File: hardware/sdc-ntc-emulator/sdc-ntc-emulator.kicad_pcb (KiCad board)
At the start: 2 copper layers, 104 x 76 mm, 33 parts, among them J1 DevKit J1, J2 DevKit J3, J3 5V IN (RAC03), J4 SDC VE1 / GND, K1 G5V-2-H1 5VDC, Q1 AO3400A, U1 ISO1540, U2 AD5272BRMZ-50

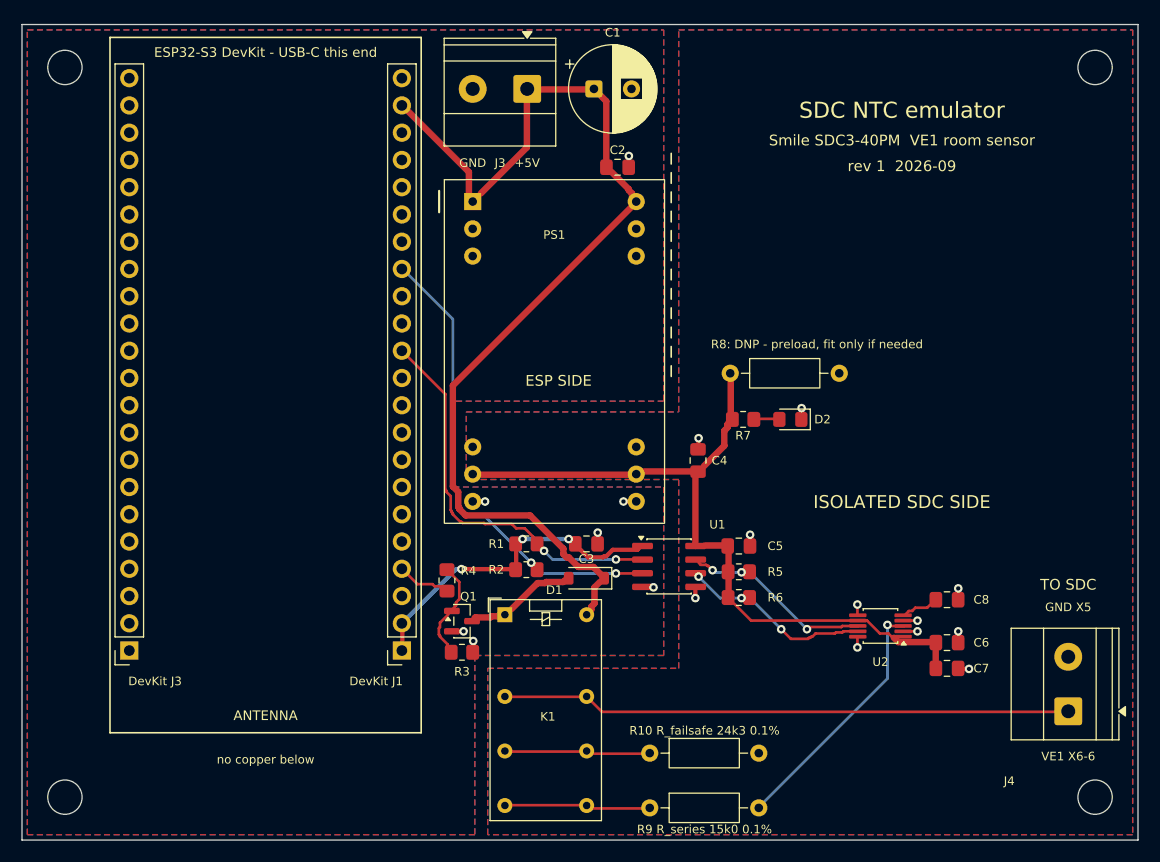
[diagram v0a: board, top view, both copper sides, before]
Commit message: PCB: fit the actual DevKit clone, fix antenna keep-out and GND split
The clone is shorter than the official DevKitC-1 and its module antenna
overhangs the DevKit edge right after pin 1, so the no-copper area now
starts there. That cut the ESP ground pour in two; an explicit GND track
from DevKit J1.22 to the TEM input ground reconnects it. Header row
spacing is now one constant (DEVKIT_ROWS, still 25.4 mm pending a
re-measurement).

Co-Authored-By: Claude Opus 5.5 <noreply@anthropic.com>
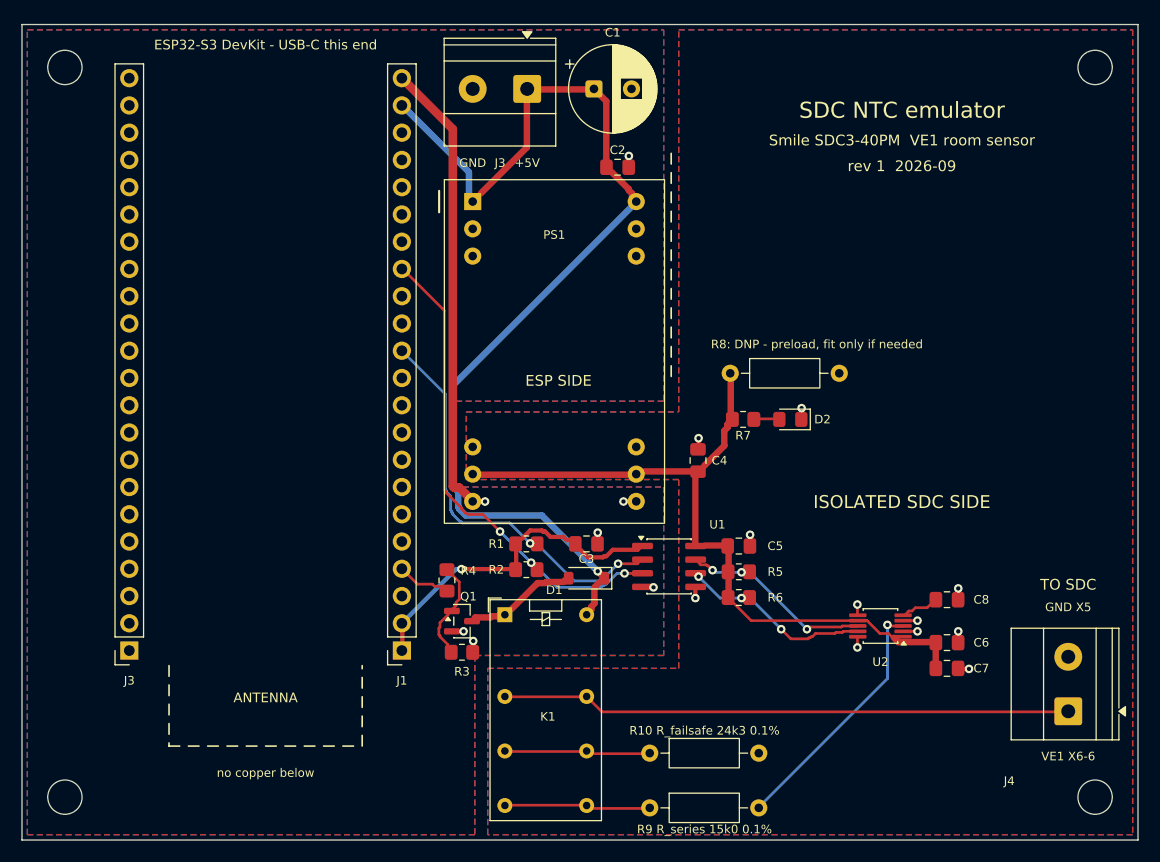
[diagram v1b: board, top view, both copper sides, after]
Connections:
- J2 pad 1: /GND -> unconnected-(J2-Pin_1-Pad1)
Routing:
- net /GND: track 7.90 -> 49.7 mm
- net /SDA_ESP: track 35.4 -> 38.0 mm
- net /SCL_ESP: track 43.9 -> 45.0 mm, vias 2 -> 3
- net /+3V3: track 27.5 -> 28.2 mm, vias 3 -> 1
- net /+5V: track 93.7 -> 93.5 mm, vias 0 -> 1
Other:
- board text added: "J1"
- board text added: "J3"
- board text removed: "DevKit J1"
- board text removed: "DevKit J3"

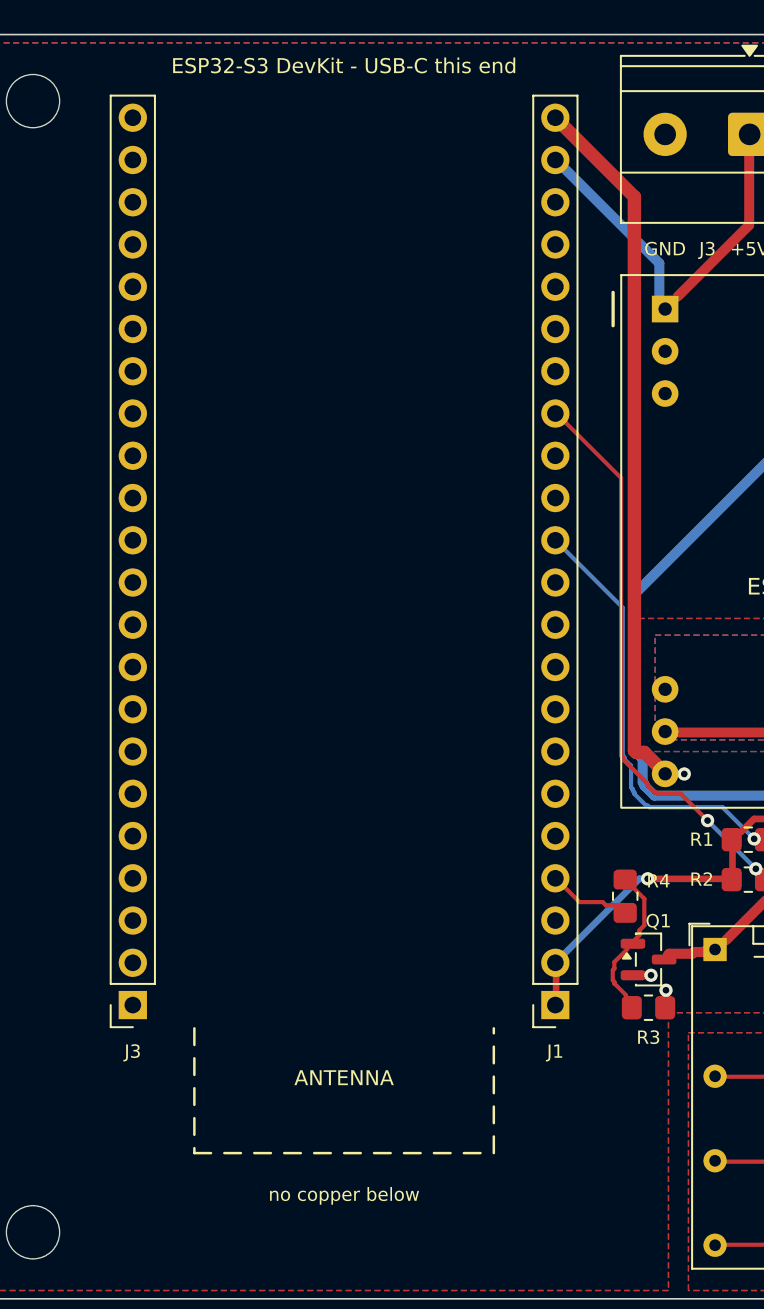
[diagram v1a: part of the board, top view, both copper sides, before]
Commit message: PCB: DevKit header rows 25.1 mm apart (measured)
Co-Authored-By: Claude Opus 5.5 <noreply@anthropic.com>
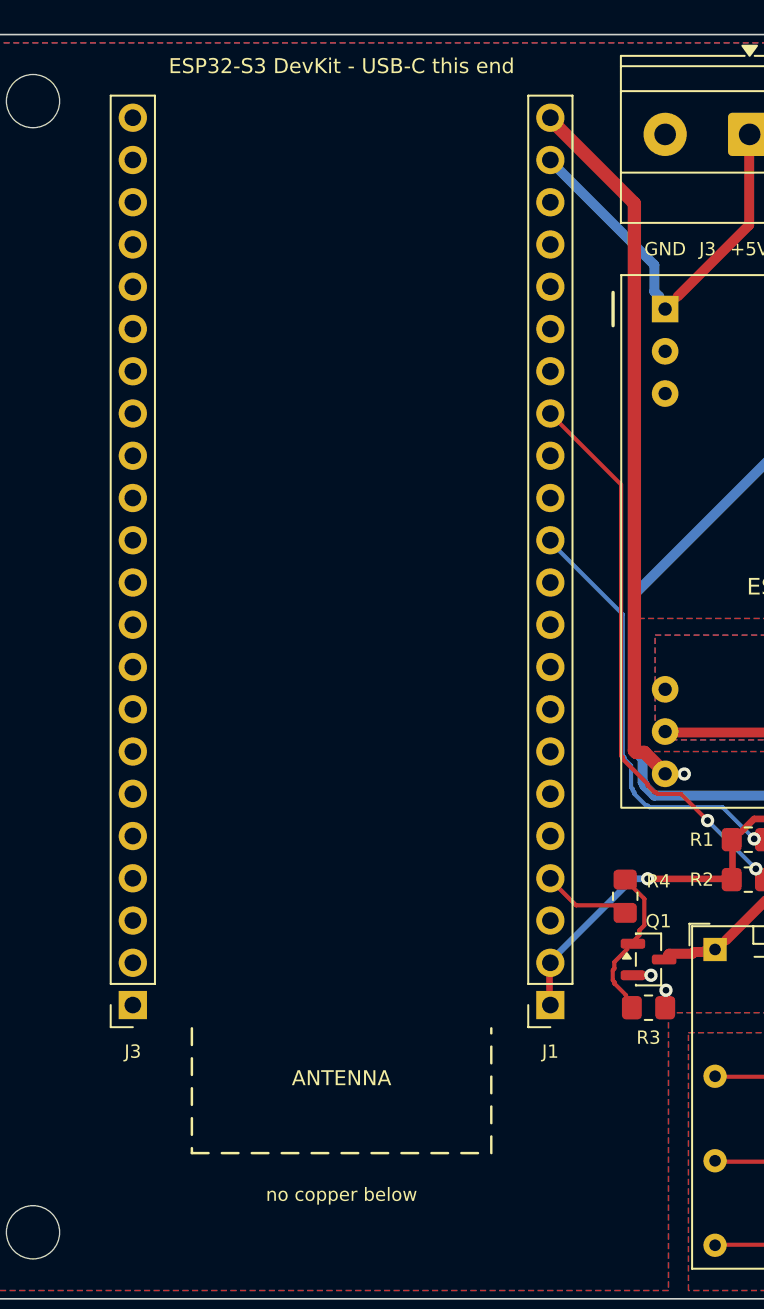
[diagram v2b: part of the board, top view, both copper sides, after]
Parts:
- moved J1 0.30 mm to (135.1, 108.3)

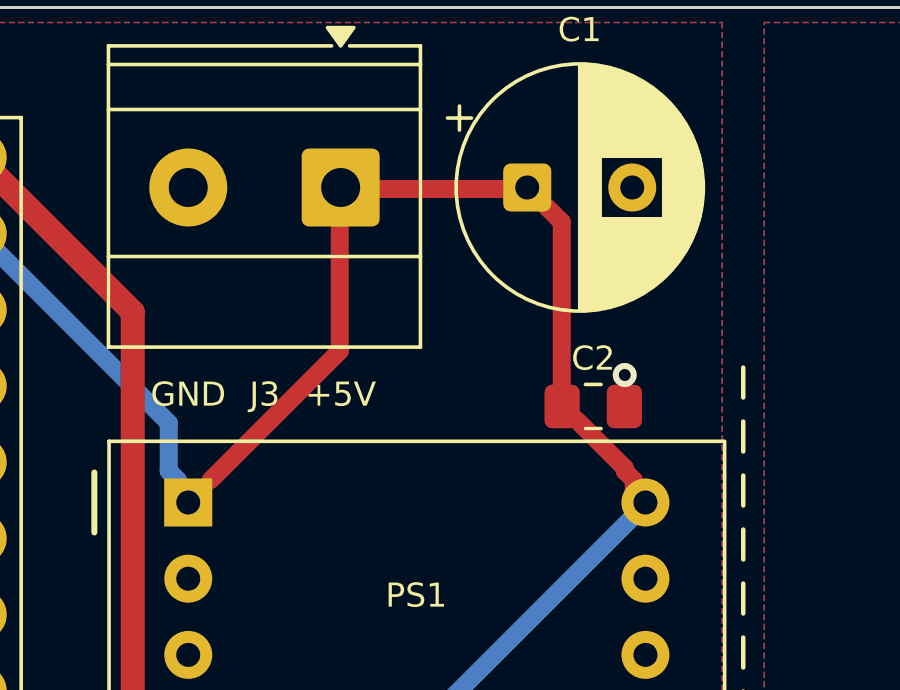
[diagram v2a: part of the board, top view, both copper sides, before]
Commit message: PCB: add 10 uF ceramic (C9) parallel to the 5 V input elco
Co-Authored-By: Claude Opus 5.5 <noreply@anthropic.com>
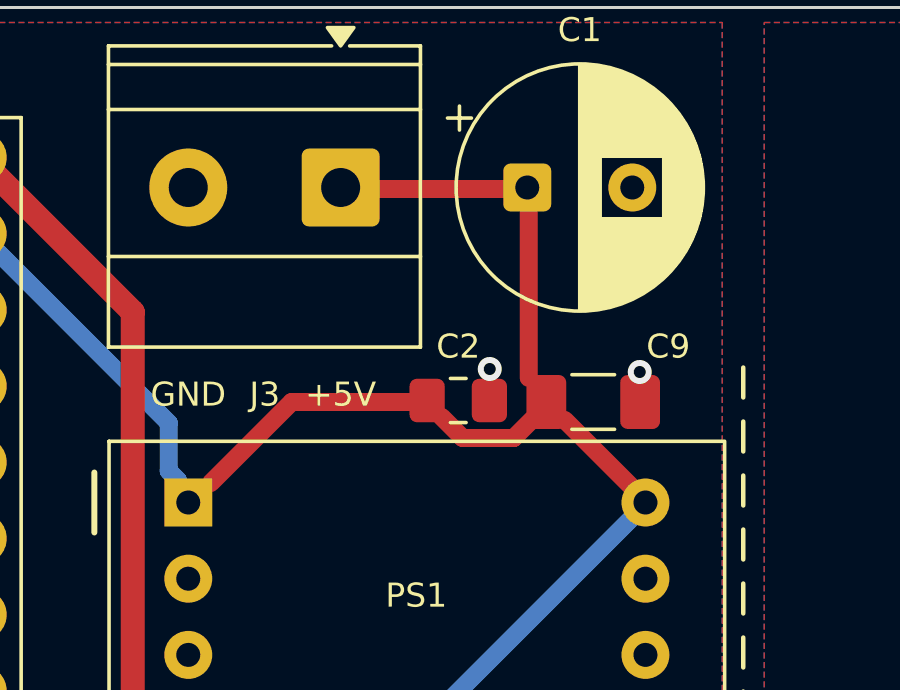
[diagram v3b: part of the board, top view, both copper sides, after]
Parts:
- added C9: 10uF 25V X7R, Capacitor_SMD:C_1206_3216Metric_Pad1.33x1.80mm_HandSolder, F.Cu at (155.5, 63.1)
- moved C2 4.50 mm to (151.0, 63.1)
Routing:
- net /+5V: track 93.5 -> 94.8 mm
- net /GND: track 49.8 -> 51.0 mm, vias 7 -> 8

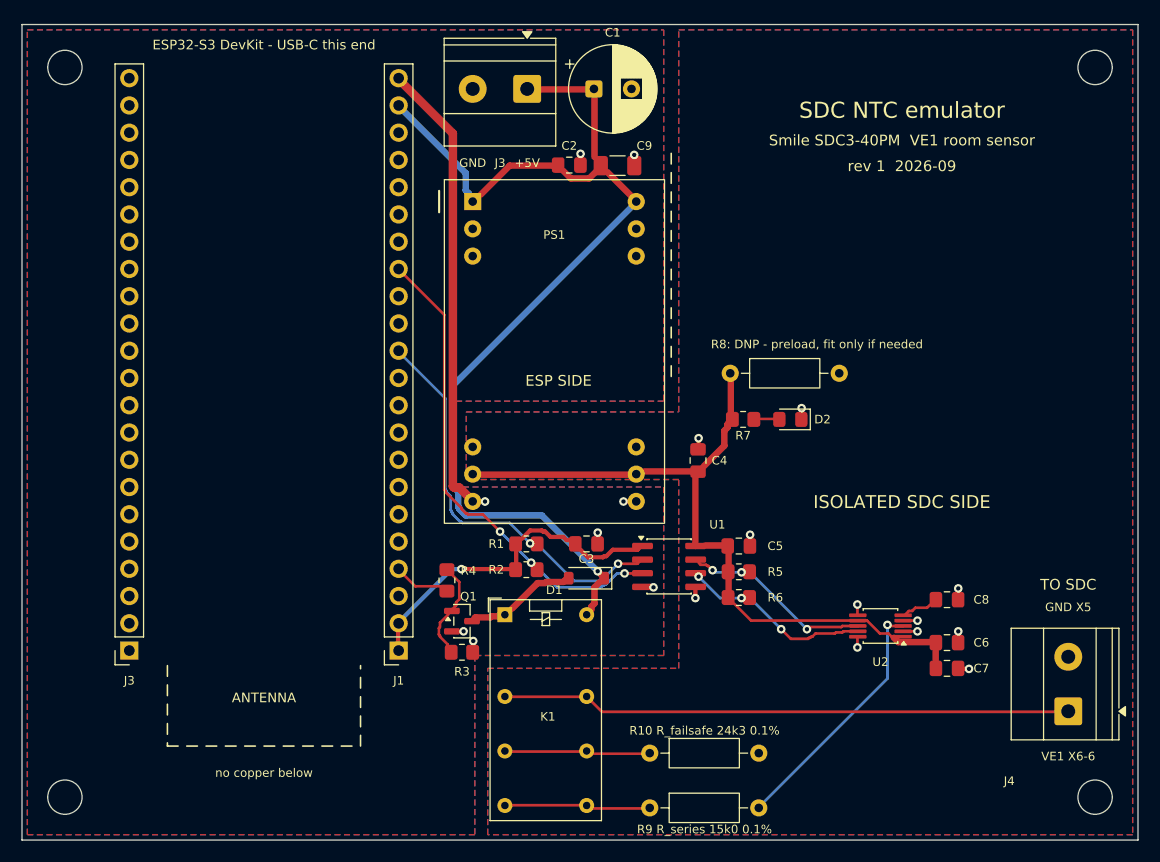
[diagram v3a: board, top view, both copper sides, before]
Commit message: PCB: move isolation gap right; C9 under DevKit at its 5V pin; C2 and R8 away from the TEM
Co-Authored-By: Claude Opus 5.5 <noreply@anthropic.com>
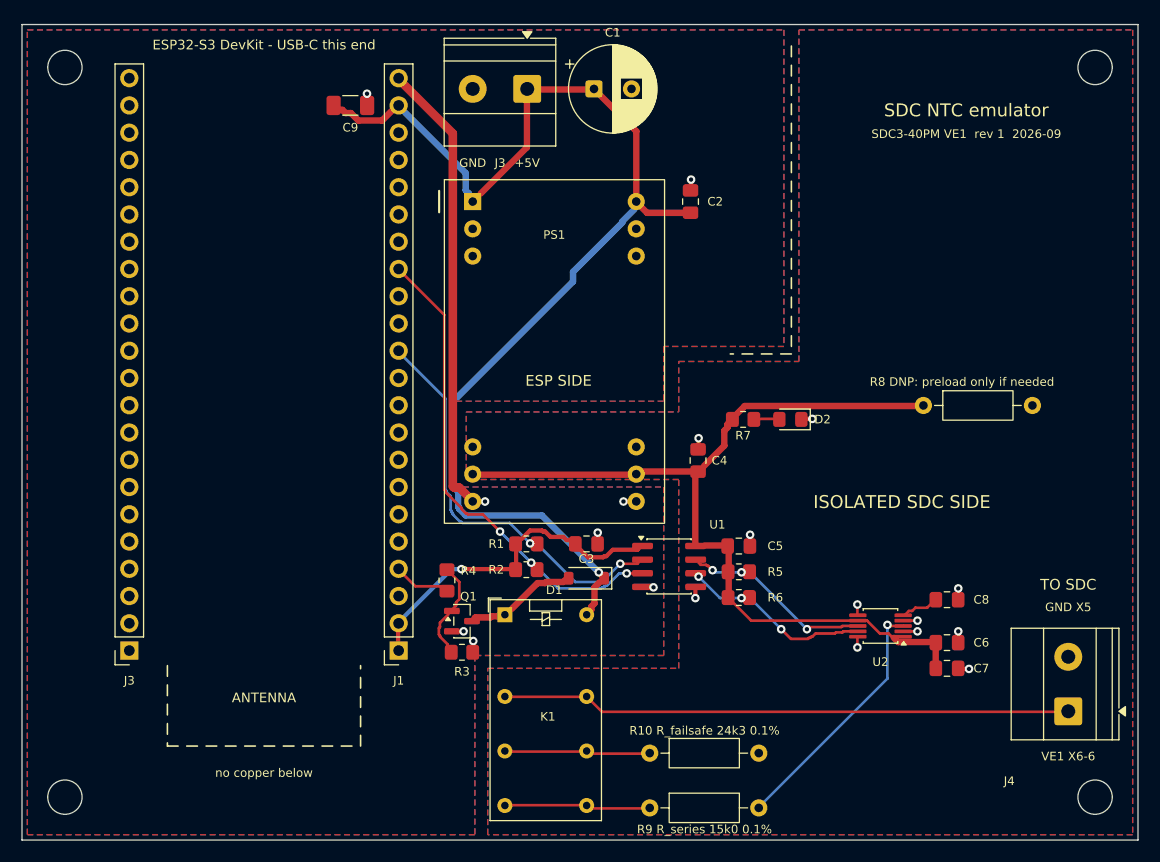
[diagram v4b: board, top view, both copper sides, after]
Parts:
- moved C9 25.5 mm to (130.6, 57.5)
- moved R8 18.2 mm to (184.0, 85.5)
- moved C2 11.8 mm to (162.3, 66.5), turned to 90 degrees
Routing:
- net /VDD_ISO: track 63.5 -> 77.6 mm
- net /+5V: track 94.8 -> 105.3 mm
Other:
- board text added: "R8 DNP: preload only if needed"
- board text added: "SDC3-40PM VE1 rev 1 2026-09"
- board text removed: "R8: DNP - preload, fit only if needed"
- board text removed: "Smile SDC3-40PM VE1 room sensor"
- board text removed: "rev 1 2026-09"

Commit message: PCB rev 2: apply the independent design review
- Isolation gap 0.40 -> 1.15 mm (oval TEM pads, wider domain outlines,
  router keeps full track width inside its domain); new
  tools/check_isolation.py measures the real copper gap and fails the build
  below 1.0 mm.
- Relay state sense (R11/R12 -> GPIO5) and reverse-polarity P-FET (Q2).
- R9 15.0k -> 18.2k (27 C floor if the AD5272 fails), R10 24.3k -> 24.9k
  (SDC +0.5 K offset), R1/R2 4.7k -> 2.7k (ISO1540 side-1 sink current).
- C3/C5 next to the ISO1540, relay holes 1.0 mm, AD5272 fan-out without
  wide tracks or vias under the chip, silkscreen >= 1.0 mm, X5-2..12 marking.
- Handoff/README: corrected X5-1, RAC03 limits, row spacing, LDO/preload
  leftovers; firmware requirements for readback, relay sense, ALWAYS_OFF.

Co-Authored-By: Claude Opus 5.5 <noreply@anthropic.com>
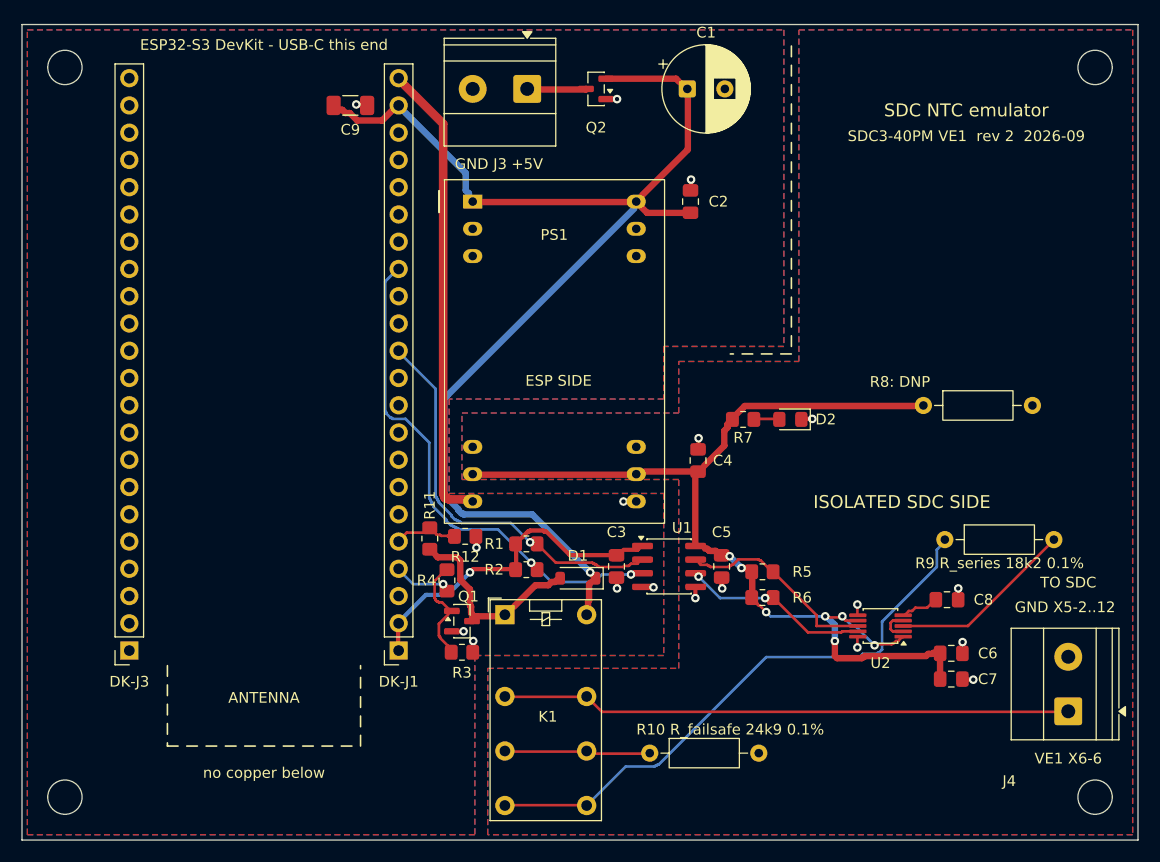
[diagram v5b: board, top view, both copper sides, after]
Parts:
- added Q2: AO3401A, Package_TO_SOT_SMD:SOT-23, F.Cu at (153.5, 56.0)
- added R11: 10k, Resistor_SMD:R_0805_2012Metric_Pad1.20x1.40mm_HandSolder, F.Cu at (138.0, 97.9)
- added R12: 20k, Resistor_SMD:R_0805_2012Metric_Pad1.20x1.40mm_HandSolder, F.Cu at (141.3, 97.7)
- C4, C7: value 10uF -> 10uF 16V X5R
- R1, R2: value 4k7 -> 2k7
- R10: value 24k3 0.1% -> 24k9 0.1% 25ppm
- R9: value 15k0 0.1% -> 18k2 0.1% 25ppm
- moved R9 37.2 mm to (186.0, 98.0)
- moved C1 8.70 mm to (162.0, 56.0)
- moved C3 3.50 mm to (155.4, 100.5), turned to -90 degrees
- moved C5 2.48 mm to (165.2, 100.5), turned to -90 degrees
- moved R5 2.20 mm to (169.0, 101.0)
- moved R6 2.20 mm to (169.0, 103.4)
- moved C6 1.08 mm to (186.6, 108.6)
- moved C7 1.08 mm to (186.6, 111.0)
- moved D1 0.80 mm to (151.8, 101.6)
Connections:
- J1 pad 5: unconnected-(J1-Pin_5-Pad5) -> /RELAY_SENSE
- J3 pad 1: /+5V -> /+5V_IN
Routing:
- net /NO_PATH: track 12.4 -> 52.2 mm
- net /VDD_ISO: track 77.6 -> 88.7 mm, vias 0 -> 7
- net /COIL_N: track 9.65 -> 17.0 mm
- net /WIPER: track 22.8 -> 16.6 mm, vias 1 -> 0
- net /+5V: track 105.3 -> 110.3 mm
- net /RELAY_SENSE: track 0.00 -> 4.71 mm
- net /+5V_IN: track 0.00 -> 4.25 mm
- net /GND: track 51.0 -> 53.8 mm, vias 8 -> 9
- net /SCL_ESP: track 45.1 -> 48.0 mm, vias 3 -> 2
- net /SDA_ESP: track 38.2 -> 36.2 mm, vias 2 -> 1
- net /SCL_ISO: track 18.2 -> 16.5 mm, vias 3 -> 2
- net /GATE: track 8.39 -> 9.16 mm
- net /GND_ISO: track 12.1 -> 12.8 mm, vias 11 -> 9
- net /SDA_ISO: track 18.0 -> 17.8 mm, vias 3 -> 0
- net /RELAY_EN: track 4.55 -> 4.73 mm, vias 0 -> 1
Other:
- board text added: "DK-J1"
- board text added: "DK-J3"
- board text added: "GND X5-2..12"
- board text added: "R10 R_failsafe 24k9 0.1%"
- board text added: "R8: DNP"
- board text added: "R9 R_series 18k2 0.1%"
- board text added: "SDC3-40PM VE1 rev 2 2026-09"
- board text removed: "GND X5"
- board text removed: "J1"
- board text removed: "J3"
- board text removed: "R10 R_failsafe 24k3 0.1%"
- board text removed: "R8 DNP: preload only if needed"
- board text removed: "R9 R_series 15k0 0.1%"
- board text removed: "SDC3-40PM VE1 rev 1 2026-09"
